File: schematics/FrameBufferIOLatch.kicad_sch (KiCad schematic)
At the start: 7 parts, among them U174 4069, U175 4069, U176 Read and FrameBuf

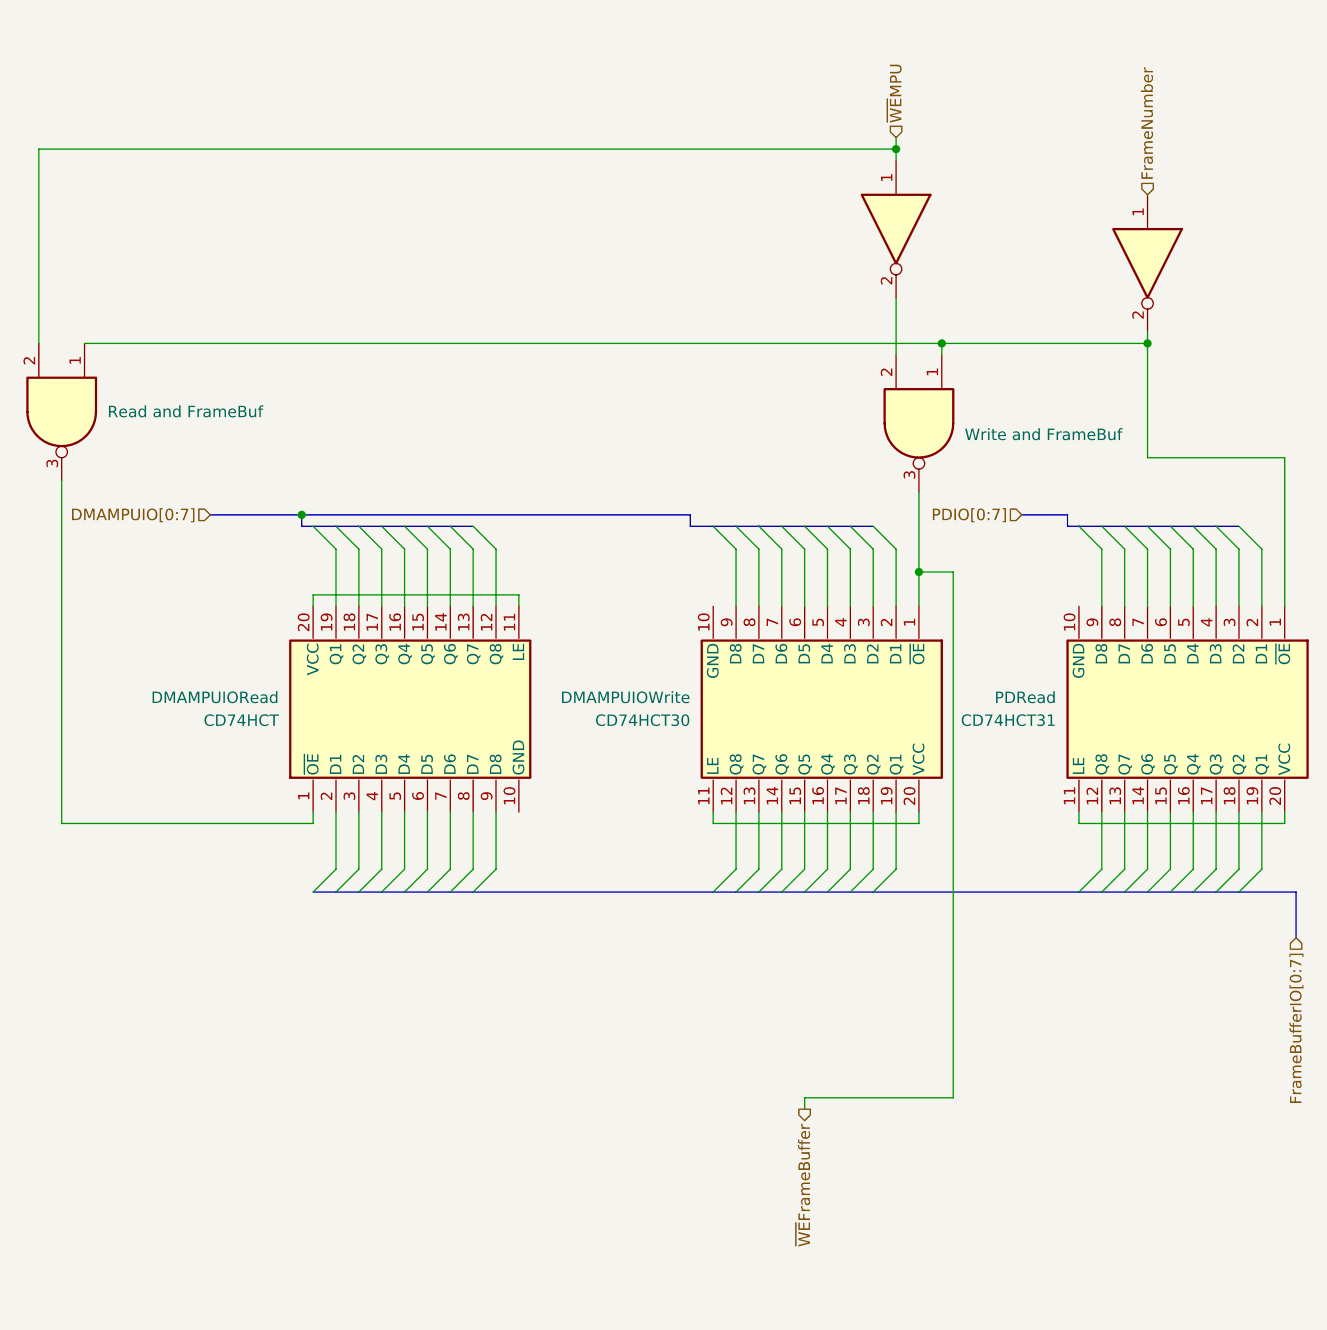
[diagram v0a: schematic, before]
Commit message: fix: assumption DMA wont write
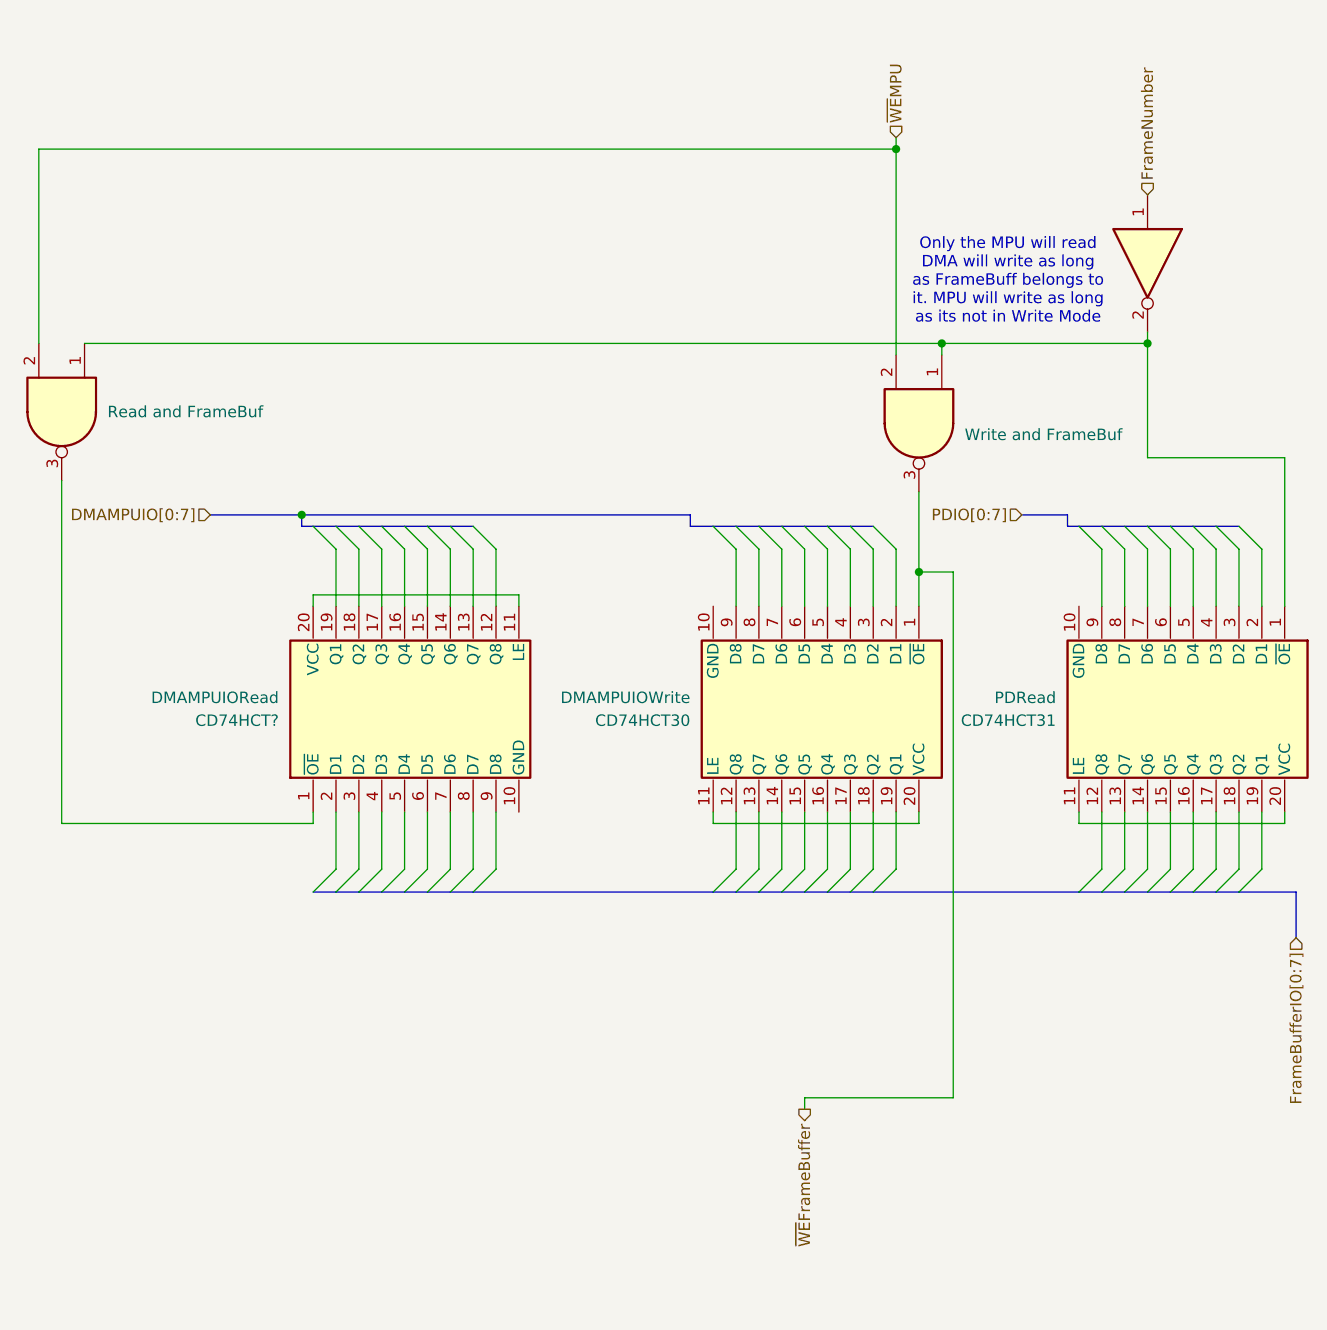
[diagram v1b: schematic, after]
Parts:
- removed U175: 4069, symbol 4xxx:4069
- renumbered CD74HCT to CD74HCT?, U to U?
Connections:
- net ~{WE}MPU: now also U?.2
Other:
- note added: "Only the MPU will read DMA will write as long as FrameBuff belongs to it. MPU will write as long as its not in Write Mode"
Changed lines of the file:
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@@
 	(generator_version "9.0")
 	(paper "A4")
+	(text "Only the MPU will read\nDMA will write as long\nas FrameBuff belongs to\nit. MPU will write as long\nas its not in Write Mode"
+		(exclude_from_sim no)
+		(at 178.816 49.022 0)
+		(effects
+			(font
+				(size 1.27 1.27)
+			)
+		)
+	)
 	(junction
 		(at 194.31 55.88)
@@
 		)
 	)
-	(wire
-		(pts
-			(xy 166.37 34.29) (xy 166.37 35.56)
-		)
-		(stroke
-			(width 0)
-			(type default)
-		)
-	)
 	(bus
 		(pts
@@
 	(wire
 		(pts
-			(xy 166.37 50.8) (xy 166.37 57.15)
+			(xy 166.37 34.29) (xy 166.37 57.15)
 		)
 		(stroke
@@
 		(dnp no)
 		(fields_autoplaced yes)
-		(property "Reference" "U"
+		(property "Reference" "U?"
 			(at 173.99 63.4916 90)
 			(effects
@@
 		(instances
 			(project "schematics"
+				(path "/1efac021-92d6-4a06-9a24-324f43ef2e7c/41bec2cb-0554-4545-a462-c7b731f22bcb"
+					(reference "U?")
+					(unit 1)
+				)
 				(path "/1efac021-92d6-4a06-9a24-324f43ef2e7c/ee9412b5-3f4d-4d26-8e91-e1a9764d02f4"
 					(reference "U172")
@@
 		(dnp no)
 		(fields_autoplaced yes)
-		(property "Reference" "CD74HCT"
+		(property "Reference" "CD74HCT?"
 			(at 97.79 97.7901 90)
 			(effects
@@
 		(instances
 			(project "schematics"
+				(path "/1efac021-92d6-4a06-9a24-324f43ef2e7c/41bec2cb-0554-4545-a462-c7b731f22bcb"
+					(reference "CD74HCT?")
+					(unit 1)
+				)
 				(path "/1efac021-92d6-4a06-9a24-324f43ef2e7c/ee9412b5-3f4d-4d26-8e91-e1a9764d02f4"
 					(reference "CD74HCT32")
 					(unit 1)
 				)
-			)
-		)
-	)
-	(symbol
-		(lib_id "4xxx:4069")
-		(at 166.37 43.18 270)
-		(unit 1)
-		(exclude_from_sim no)
-		(in_bom yes)
-		(on_board yes)
-		(dnp no)
-		(fields_autoplaced yes)
-		(property "Reference" "U175"
-			(at 157.48 43.18 0)
-			(effects
-				(font
-					(size 1.27 1.27)
-				)
-				(hide yes)
-			)
-		)
-		(property "Value" "4069"
-			(at 160.02 43.18 0)
-			(effects
-				(font
-					(size 1.27 1.27)
-				)
-				(hide yes)
-			)
-		)
-		(property "Footprint" ""
-			(at 166.37 43.18 0)
-			(effects
-				(font
-					(size 1.27 1.27)
-				)
-				(hide yes)
-			)
-		)
-		(property "Datasheet" "http://www.intersil.com/content/dam/Intersil/documents/cd40/cd4069ubms.pdf"
-			(at 166.37 43.18 0)
-			(effects
-				(font
-					(size 1.27 1.27)
-				)
-				(hide yes)
-			)
-		)
-		(property "Description" "Hex inverter"
-			(at 166.37 43.18 0)
-			(effects
-				(font
-					(size 1.27 1.27)
-				)
-				(hide yes)
-			)
-		)
-		(pin "5"
-		)
-		(pin "4"
-		)
-		(pin "13"
-		)
-		(pin "6"
-		)
-		(pin "8"
-		)
-		(pin "3"
-		)
-		(pin "7"
-		)
-		(pin "12"
-		)
-		(pin "14"
-		)
-		(pin "11"
-		)
-		(pin "9"
-		)
-		(pin "1"
-		)
-		(pin "10"
-		)
-		(pin "2"
-		)
-		(instances
-			(project "schematics"
-				(path "/1efac021-92d6-4a06-9a24-324f43ef2e7c/41bec2cb-0554-4545-a462-c7b731f22bcb"
-					(reference "U175")
-					(unit 1)
-				)
-				(path "/1efac021-92d6-4a06-9a24-324f43ef2e7c/ee9412b5-3f4d-4d26-8e91-e1a9764d02f4"
-					(reference "U15")
-					(unit 1)
-				)
